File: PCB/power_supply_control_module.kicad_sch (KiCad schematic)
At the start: 39 parts, among them J1 ICSP, J2 USB_X, J3 PS_POT, J4 POWER, J5 DISP, J6 USB_Y, J7 USB_A, SW1 Voltage, SW2 Current, SW3 Voltage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

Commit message: [SW] debounced buttons added
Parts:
- SW3, SW4: Field5 (none) -> EC12E
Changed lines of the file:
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@@
 		(on_board yes)
 		(dnp no)
-		(fields_autoplaced yes)
 		(property "Reference" "SW4"
 			(at 104.14 137.1599 0)
@@
 			)
 		)
-		(property "Field5" ""
-			(at 97.79 138.43 0)
+		(property "Field5" "EC12E"
+			(at 107.442 142.494 0)
 			(effects
 				(font
 					(size 1.27 1.27)
 				)
-				(hide yes)
 			)
 		)
@@
 		(on_board yes)
 		(dnp no)
-		(fields_autoplaced yes)
 		(property "Reference" "SW3"
 			(at 104.14 119.3799 0)
@@
 			)
 		)
-		(property "Field5" ""
+		(property "Field5" "EC12E"
+			(at 107.442 124.714 0)
+			(effects
+				(font
+					(size 1.27 1.27)
+				)
+			)
+		)
+		(property "Field6" ""
 			(at 97.79 120.65 0)
 			(effects

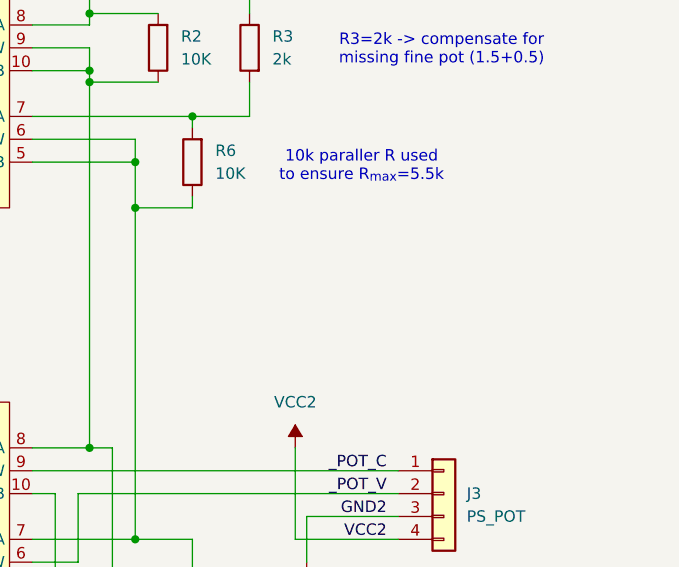
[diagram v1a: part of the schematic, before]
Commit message: successfully setting voltage and current
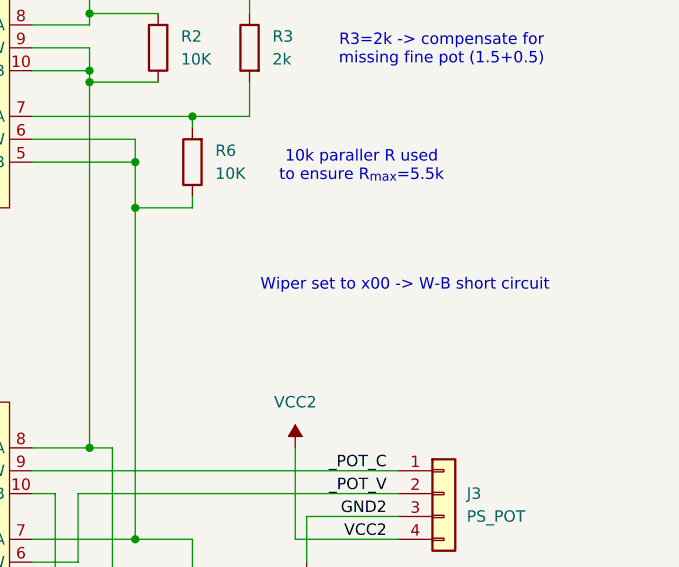
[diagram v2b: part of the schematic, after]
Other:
- note added: "Wiper set to x00 -> W-B short circuit"
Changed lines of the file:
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@@
+		)
+	)
+	(text "Wiper set to x00 -> W-B short circuit "
+		(exclude_from_sim no)
+		(at 254.762 87.376 0)
+		(effects
+			(font
+				(size 1.27 1.27)
+			)
 		)
 	)
